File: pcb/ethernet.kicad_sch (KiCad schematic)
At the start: 42 parts, among them U9 W5500, Y1 25MHz

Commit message: sch: replace hanrun ethernet jack with one rated for lower temperature
This board will likely end up in places that are quite cold, so there is a need to use a lower temperature rated ethernet jack since the HanRun one was only rated down to 0C
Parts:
- removed D2: HR915310A, EasyEDA:RJ45-TH_HR915310A, symbol EasyEDA:HR915310A
- added RJ1: GR01M1HXA001, EasyEDA:RJ45-TH_GR01M1HXA001, symbol EasyEDA:GR01M1HXA001
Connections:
- net +3V3: now also RJ1.12, RJ1.9
- net CGND: now also RJ1.8, RJ1.SH
- net RCT: now also RJ1.5 (RCT)
- net RD+: now also RJ1.6 (RD+)
- net RD-: now also RJ1.7 (RD-)
- net TCT: now also RJ1.3 (TCT)
- net TD+: now also RJ1.1 (TD+)
- net TD-: now also RJ1.2 (TD-)
- net at R46.1: now also RJ1.11
- net at R47.1: now also RJ1.10
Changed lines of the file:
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@@
 	)
 	(symbol
+		(lib_id "EasyEDA:GR01M1HXA001")
+		(at 233.68 44.45 0)
+		(unit 1)
+		(body_style 1)
+		(exclude_from_sim no)
+		(in_bom yes)
+		(on_board yes)
+		(in_pos_files yes)
+		(dnp no)
+		(fields_autoplaced yes)
+		(property "Reference" "RJ1"
+			(at 234.95 30.48 0)
+			(show_name no)
+			(do_not_autoplace no)
+			(effects
+				(font
+					(size 1.27 1.27)
+				)
+			)
+		)
+		(property "Value" "GR01M1HXA001"
+			(at 234.95 33.02 0)
+			(show_name no)
+			(do_not_autoplace no)
+			(effects
+				(font
+					(size 1.27 1.27)
+				)
+			)
+		)
+		(property "Footprint" "EasyEDA:RJ45-TH_GR01M1HXA001"
+			(at 233.68 68.58 0)
+			(hide yes)
+			(show_name no)
+			(do_not_autoplace no)
+			(effects
+				(font
+					(size 1.27 1.27)
+				)
+			)
+		)
+		(property "Datasheet" "https://www.lcsc.com/datasheet/C4155019.pdf"
+			(at 233.68 71.12 0)
+			(hide yes)
+			(show_name no)
+			(do_not_autoplace no)
+			(effects
+				(font
+					(size 1.27 1.27)
+				)
+			)
+		)
+		(property "Description" ""
+			(at 158.115 45.085 0)
+			(hide yes)
+			(show_name no)
+			(do_not_autoplace no)
+			(effects
+				(font
+					(size 1.27 1.27)
+				)
+			)
+		)
+		(property "Manufacturer" "E-NETTR(祥星电子)"
+			(at 233.68 73.66 0)
+			(hide yes)
+			(show_name no)
+			(do_not_autoplace no)
+			(effects
+				(font
+					(size 1.27 1.27)
+				)
+			)
+		)
+		(property "MPN" "GR01M1HXA001"
+			(at 233.68 76.2 0)
+			(hide yes)
+			(show_name no)
+			(do_not_autoplace no)
+			(effects
+				(font
+					(size 1.27 1.27)
+				)
+			)
+		)
+		(property "LCSC Part" "C4155019"
+			(at 233.68 78.74 0)
+			(hide yes)
+			(show_name no)
+			(do_not_autoplace no)
+			(effects
+				(font
+					(size 1.27 1.27)
+				)
+			)
+		)
+		(pin "4"
+		)
+		(pin "3"
+		)
+		(pin "2"
+		)
+		(pin "5"
+		)
+		(pin "1"
+		)
+		(pin "11"
+		)
+		(pin "12"
+		)
+		(pin "6"
+		)
+		(pin "SH"
+		)
+		(pin "7"
+		)
+		(pin "9"
+		)
+		(pin "10"
+		)
+		(pin "8"
+		)
+		(instances
+			(project "EveningStar"
+				(path "/4c61f5a2-f8d4-462a-9bc3-d74437d30372/561d5dbe-6020-48c7-be42-1a6149a1119b"
+					(reference "RJ1")
+					(unit 1)
+				)
+			)
+		)
+	)
+	(symbol
 		(lib_id "power:GND")
 		(at 128.27 36.83 0)
@@
 					(unit 1)
 				)
-			)
-		)
-	)
-	(symbol
-		(lib_id "EasyEDA:HR915310A")
-		(at 234.95 44.45 0)
-		(unit 1)
-		(body_style 1)
-		(exclude_from_sim no)
-		(in_bom yes)
-		(on_board yes)
-		(in_pos_files yes)
-		(dnp no)
-		(property "Reference" "D2"
-			(at 235.204 30.734 0)
-			(show_name no)
-			(do_not_autoplace no)
-			(effects
-				(font
-					(size 1.27 1.27)
-				)
-			)
-		)
-		(property "Value" "HR915310A"
-			(at 235.204 33.274 0)
-			(show_name no)
-			(do_not_autoplace no)
-			(effects
-				(font
-					(size 1.27 1.27)
-				)
-			)
-		)
-		(property "Footprint" "EasyEDA:RJ45-TH_HR915310A"
-			(at 234.95 72.39 0)
-			(hide yes)
-			(show_name no)
-			(do_not_autoplace no)
-			(effects
-				(font
-					(size 1.27 1.27)
-				)
-			)
-		)
-		(property "Datasheet" "https://www.lcsc.com/datasheet/C2760326.pdf"
-			(at 234.95 74.93 0)
-			(hide yes)
-			(show_name no)
-			(do_not_autoplace no)
-			(effects
-				(font
-					(size 1.27 1.27)
-				)
-			)
-		)
-		(property "Description" ""
-			(at 234.95 44.45 0)
-			(hide yes)
-			(show_name no)
-			(do_not_autoplace no)
-			(effects
-				(font
-					(size 1.27 1.27)
-				)
-			)
-		)
-		(property "Manufacturer" "HANRUN(汉仁)"
-			(at 234.95 77.47 0)
-			(hide yes)
-			(show_name no)
-			(do_not_autoplace no)
-			(effects
-				(font
-					(size 1.27 1.27)
-				)
-			)
-		)
-		(property "MPN" "HR915310A"
-			(at 234.95 80.01 0)
-			(hide yes)
-			(show_name no)
-			(do_not_autoplace no)
-			(effects
-				(font
-					(size 1.27 1.27)
-				)
-			)
-		)
-		(property "LCSC Part" "C2760326"
-			(at 234.95 82.55 0)
-			(hide yes)
-			(show_name no)
-			(do_not_autoplace no)
-			(effects
-				(font
-					(size 1.27 1.27)
-				)
-			)
-		)
-		(pin "11"
-		)
-		(pin "10"
-		)
-		(pin "12"
-		)
-		(pin "5"
-		)
-		(pin "8"
-		)
-		(pin "2"
-		)
-		(pin "1"
-		)
-		(pin "4"
-		)
-		(pin "3"
-		)
-		(pin "SH"
-		)
-		(pin "7"
-		)
-		(pin "6"
-		)
-		(pin "9"
-		)
-		(instances
-			(project "EveningStar"
-				(path "/4c61f5a2-f8d4-462a-9bc3-d74437d30372/561d5dbe-6020-48c7-be42-1a6149a1119b"
-					(reference "D2")
-					(unit 1)
-				)

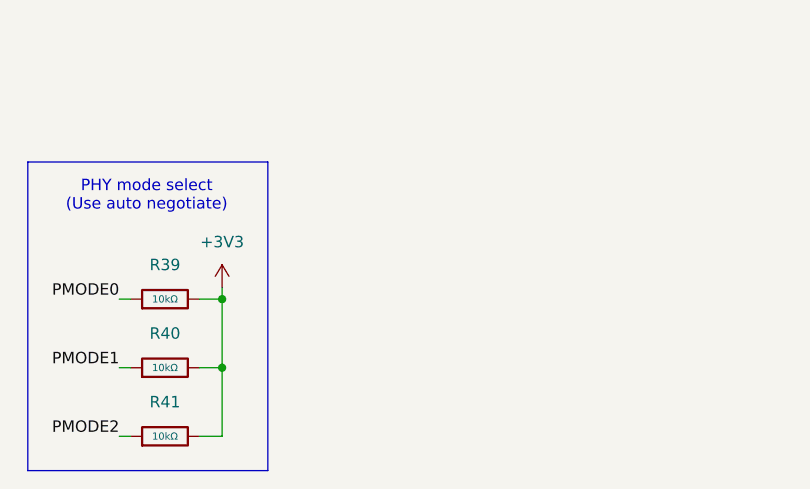
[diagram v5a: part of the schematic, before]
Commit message: sch: adjust test points
Removes some test points, and adds useful ones to data lines. Fixes #19
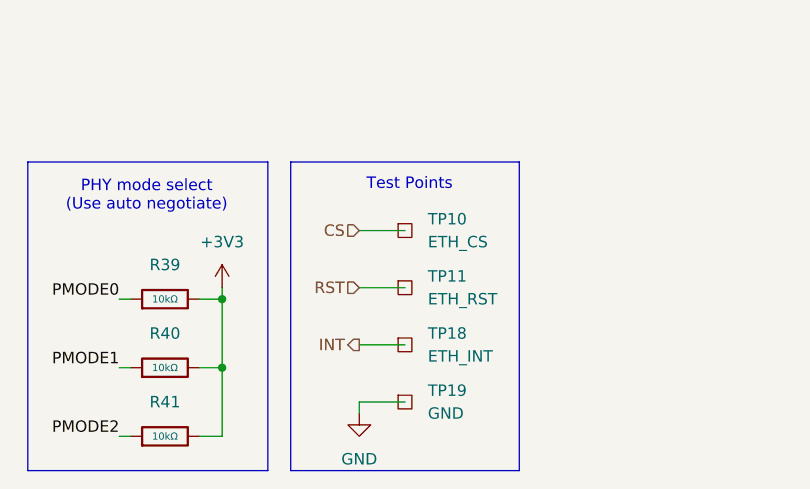
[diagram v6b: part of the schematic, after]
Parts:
- added TP10: ETH_CS, TestPoint:TestPoint_Pad_D1.0mm, symbol Connector:TestPoint_Square
- added TP11: ETH_RST, TestPoint:TestPoint_Pad_D1.0mm, symbol Connector:TestPoint_Square
- added TP18: ETH_INT, TestPoint:TestPoint_Pad_D1.0mm, symbol Connector:TestPoint_Square
- added TP19: GND, TestPoint:TestPoint_Plated_Hole_D2.0mm, symbol Connector:TestPoint_Square
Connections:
- net CS: now also TP10.1
- net GND: now also TP19.1
- net INT: now also TP18.1
- net RST: now also TP11.1
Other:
- note added: "Test Points"

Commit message: sch: add schematic titles and do some cleanup
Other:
- company: (none) -> CIA Assured
- title: (none) -> Ethernet
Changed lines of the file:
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@@
 	(generator_version "10.0")
 	(paper "A4")
+	(title_block
+		(title "Ethernet")
+		(company "CIA Assured")
+	)
 	(rectangle
 		(start 55.88 161.29)
